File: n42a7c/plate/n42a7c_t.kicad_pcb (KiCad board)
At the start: 2 copper layers, 265.5 x 105.1 mm, 46 parts, among them SW1 CPG151101S11-16, SW10 CPG151101S11-16, SW11 CPG151101S11-16, SW12 CPG151101S11-16, SW13 CPG151101S11-16, SW14 CPG151101S11-16, SW15 CPG151101S11-16, SW16 CPG151101S11-16, SW17 CPG151101S11-16, SW18 CPG151101S11-16, SW19 CPG151101S11-16, SW2 CPG151101S11-16, SW20 CPG151101S11-16, SW21 CPG151101S11-16, SW22 CPG151101S11-16, SW23 CPG151101S11-16, SW24 CPG151101S11-16, SW25 CPG151101S11-16, SW26 CPG151101S11-16, SW27 CPG151101S11-16, SW28 CPG151101S11-16, SW29 CPG151101S11-16, SW3 CPG151101S11-16, SW30 CPG151101S11-16, SW31 CPG151101S11-16, SW32 CPG151101S11-16, SW33 CPG151101S11-16, SW34 CPG151101S11-16, SW35 CPG151101S11-16, SW36 CPG151101S11-16, SW37 CPG151101S11-16, SW38 CPG151101S11-16, SW39 CPG151101S11-16, SW4 CPG151101S11-16, SW40 CPG151101S11-16, SW41 CPG151101S11-16, SW42 CPG151101S11-16, SW5 CPG151101S11-16, SW6 CPG151101S11-16, SW7 CPG151101S11-16, SW8 CPG151101S11-16, SW9 CPG151101S11-16

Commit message: create plate / production PCB
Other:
- board text added: "7.0mm spacer"
- board text added: "CON"
- board text added: "M3x5 ramimate"
- board text added: "PHconn SMD"
- board text added: "foot"
- board text removed: "Fn"

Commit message: create plate/production PCB
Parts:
- moved SW35 2.38 mm to (30.4, 105.4)
- moved SW36 2.38 mm to (54.2, 105.4)
- moved SW41 2.38 mm to (238.7, 105.4)
- moved SW42 2.38 mm to (262.5, 105.4)
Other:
- outline, holes or cut-outs redrawn
- board text added: "n42a7c Rev 1.1 Jul. 2025 Designed by @_hatano_"
- board text removed: "n42a7c Rev 1.0 Jun. 2025 Designed by @_hatano_"
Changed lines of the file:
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@@
 	(footprint "cscslib:CPG151101S11_frame"
 		(layer "B.Cu")
-		(at 260.151781 105.370401)
+		(at 262.532592 105.370401)
 		(property "Reference" "SW42"
 			(at 0 0 180)
@@
 	(footprint "cscslib:CPG151101S11_frame"
 		(layer "B.Cu")
-		(at 236.339261 105.370401)
+		(at 238.720112 105.370224)
 		(property "Reference" "SW41"
 			(at 0 0 180)
@@
 	(footprint "cscslib:CPG151101S11_frame"
 		(layer "B.Cu")
-		(at 32.742215 105.370404)
+		(at 30.360912 105.370404)
 		(property "Reference" "SW35"
 			(at 0 0 180)
@@
 	(footprint "cscslib:CPG151101S11_frame"
 		(layer "B.Cu")
-		(at 56.554735 105.370401)
+		(at 54.173432 105.370401)
 		(property "Reference" "SW36"
 			(at 0 0 180)
@@
 	)
 	(gr_circle
-		(center 23.217207 111.323531)
-		(end 27.217207 111.323531)
+		(center 21.431232 111.323344)
+		(end 25.431232 111.323344)
 		(stroke
 			(width 0.15)
@@
 	)
 	(gr_circle
-		(center 269.676789 111.323531)
-		(end 273.676789 111.323531)
+		(center 271.462272 111.323344)
+		(end 275.462272 111.323344)
 		(stroke
 			(width 0.15)
@@
 		)
 		(fill no)
+		(layer "Eco2.User")
+	)
+	(gr_line
+		(start 173.533448 22.621875)
+		(end 155.078776 22.621875)
+		(stroke
+			(width 0.15)
+			(type solid)
+		)
 		(layer "Eco2.User")
 	)
@@
 	(gr_line
 		(start 252.114181 117.276667)
-		(end 273.843481 117.276466)
+		(end 276.224768 117.276466)
 		(stroke
 			(width 0.15)
@@
 	(gr_line
 		(start 279.201797 97.036019)
-		(end 274.439293 116.68151)
+		(end 276.82008 116.68151)
 		(stroke
 			(width 0.15)
@@
 	)
 	(gr_arc
-		(start 19.049886 117.270465)
-		(mid 18.628987 117.096118)
-		(end 18.454639 116.675221)
+		(start 16.668722 117.276417)
+		(mid 16.247823 117.10207)
+		(end 16.073475 116.681173)
 		(stroke
 			(width 0.15)
@@
 	(gr_line
 		(start 40.78259 117.27626)
-		(end 19.049886 117.270464)
+		(end 16.668736 117.270464)
 		(stroke
 			(width 0.15)
@@
 	)
 	(gr_arc
-		(start 274.439268 116.681329)
-		(mid 274.264716 117.102069)
-		(end 273.843955 117.276642)
+		(start 276.820736 116.681881)
+		(mid 276.646184 117.102621)
+		(end 276.225423 117.277194)
 		(stroke
 			(width 0.15)
@@
 	(gr_line
 		(start 13.692199 97.036019)
-		(end 18.454638 116.6753)
+		(end 16.073424 116.675221)
 		(stroke
 			(width 0.15)
@@
 		(layer "Edge.Cuts")
 	)
-	(gr_text "n42a7c Rev 1.0 Jun. 2025\nDesigned by @_hatano_"
+	(gr_text "n42a7c Rev 1.1 Jul. 2025\nDesigned by @_hatano_"
 		(at 204.192359 36.314113 0)
 		(layer "F.SilkS")
@@
 		(layer "Dwgs.User")
 		(pts
-			(xy 196.750616 22.621875) (xy 248.245104 127.695054)
+			(xy 199.131427 22.621875) (xy 250.625915 127.695054)
 		)
 		(height 88.999144)
@@
 		)
 		(gr_text "105.07"
-			(at 284.59976 75.158465 90)
-			(layer "Dwgs.User")
-			(effects
+			(at 286.980571 75.158465 90)
+			(layer "Dwgs.User")
+			(effects

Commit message: create production plate
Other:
- outline, holes or cut-outs redrawn
- board text added: "JLCJLCJLCJLC"
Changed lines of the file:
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@@
 		(layer "F.SilkS")
+	)
+	(gr_circle
+		(center 175.914696 23.217168)
+		(end 175.61704 23.217168)
+		(stroke
+			(width 0.15)
+			(type solid)
+		)
+		(fill yes)
+		(layer "B.SilkS")
 	)
 	(gr_poly
@@
 	)
 	(gr_circle
-		(center 183.356096 36.611688)
-		(end 183.951408 36.611688)
-		(stroke
-			(width 0.1)
-			(type default)
-		)
-		(fill no)
-		(layer "Cmts.User")
-	)
-	(gr_circle
-		(center 185.210784 37.611688)
-		(end 185.737343 37.611688)
-		(stroke
-			(width 0.1)
-			(type solid)
-		)
-		(fill no)
-		(layer "Cmts.User")
-	)
-	(gr_circle
 		(center 153.590625 104.775)
 		(end 154.781252 104.775002)
@@
 		(layer "Eco2.User")
 	)
-	(gr_rect
-		(start 175.060784 32.011688)
-		(end 187.060784 41.211688)
-		(stroke
-			(width 0.15)
-			(type solid)
-		)
-		(fill no)
-		(locked yes)
-		(layer "Eco2.User")
-	)
 	(gr_circle
 		(center 269.081476 41.67191)
@@
 		(layer "Eco2.User")
 	)
+	(gr_line
+		(start 173.533448 44.053088)
+		(end 173.533449 22.621856)
+		(stroke
+			(width 0.15)
+			(type solid)
+		)
+		(layer "Eco2.User")
+	)
 	(gr_circle
 		(center 21.431232 111.323344)
@@
 	)
 	(gr_rect
-		(start 175.060784 33.161688)
-		(end 187.060784 40.061688)
+		(start 175.656096 33.161688)
+		(end 187.656096 40.061688)
 		(stroke
 			(width 0.15)
@@
 		(start 237.827144 35.71872)
 		(end 230.088088 35.718779)
+		(stroke
+			(width 0.15)
+			(type solid)
+		)
+		(layer "Eco2.User")
+	)
+	(gr_line
+		(start 155.078776 22.621856)
+		(end 155.078776 44.053088)
 		(stroke
 			(width 0.15)
@@
 	)
 	(gr_line
-		(start 173.533448 22.621875)
-		(end 155.078776 22.621875)
+		(start 155.078776 44.053088)
+		(end 173.533448 44.053088)
 		(stroke
 			(width 0.15)
@@
 	)
 	(gr_line
-		(start 173.533448 44.053088)
-		(end 173.533449 22.621856)
-		(stroke
-			(width 0.15)
-			(type solid)
-		)
-		(layer "Edge.Cuts")
-	)
-	(gr_line
 		(start 252.114181 117.276667)
 		(end 276.224768 117.276466)
@@
 	)
 	(gr_line
-		(start 155.078776 22.621856)
-		(end 155.078776 44.053088)
-		(stroke
-			(width 0.15)
-			(type solid)
-		)
-		(layer "Edge.Cuts")
-	)
-	(gr_line
 		(start 96.142888 22.621894)
 		(end 146.446752 22.621894)
@@
 	)
 	(gr_line
+		(start 173.533448 22.621875)
+		(end 155.078776 22.621875)
+		(stroke
+			(width 0.15)
+			(type solid)
+		)
+		(layer "Edge.Cuts")
+	)
+	(gr_line
 		(start 48.540019 117.276628)
 		(end 79.176629 117.276663)
@@
 			(width 0.15)
 			(type default)
-		)
-		(layer "Edge.Cuts")
-	)
-	(gr_line
-		(start 155.078776 44.053088)
-		(end 173.533448 44.053088)
-		(stroke
-			(width 0.15)
-			(type solid)
 		)
 		(layer "Edge.Cuts")
@@
 		)
 	)
-	(gr_text "POWER"
-		(at 180.677192 23.514824 0)
+	(gr_text "JLCJLCJLCJLC"
+		(at 164.30625 27.384375 0)
 		(layer "F.SilkS")
 		(effects
@@
 		)
 	)
-	(gr_text "PON"
-		(at 194.071712 23.81248 0)
-		(layer "F.SilkS" knockout)
+	(gr_text "7.0mm\nspacer"
+		(at 254 144.85 0)
+		(layer "Dwgs.User")
 		(effects
 			(font
@@
 		)
 	)
-	(gr_text "CON"
-		(at 188.416248 23.81248 0)
-		(layer "F.SilkS" knockout)
+	(gr_text "POWER"
+		(at 180.677192 23.514824 0)
+		(layer "Dwgs.User")
 		(effects
 			(font
@@
 		)
 	)
-	(gr_text "7.0mm\nspacer"
-		(at 254 144.85 0)
+	(gr_text "foot"
+		(at 262.5 151.2 0)
 		(layer "Dwgs.User")
 		(effects
@@
 		)
 	)
-	(gr_text "foot"
-		(at 262.5 151.2 0)
-		(layer "Dwgs.User")
+	(gr_text "PON"
+		(at 194.071712 23.81248 0)
+		(layer "Dwgs.User" knockout)
 		(effects
 			(font
@@
 		(effects
 			(font
+				(size 1 1)
+				(thickness 0.15)
+			)
+		)
+	)
+	(gr_text "CON"
+		(at 188.416248 23.81248 0)
+		(layer "Dwgs.User" knockout)
+		(effects
+			(font

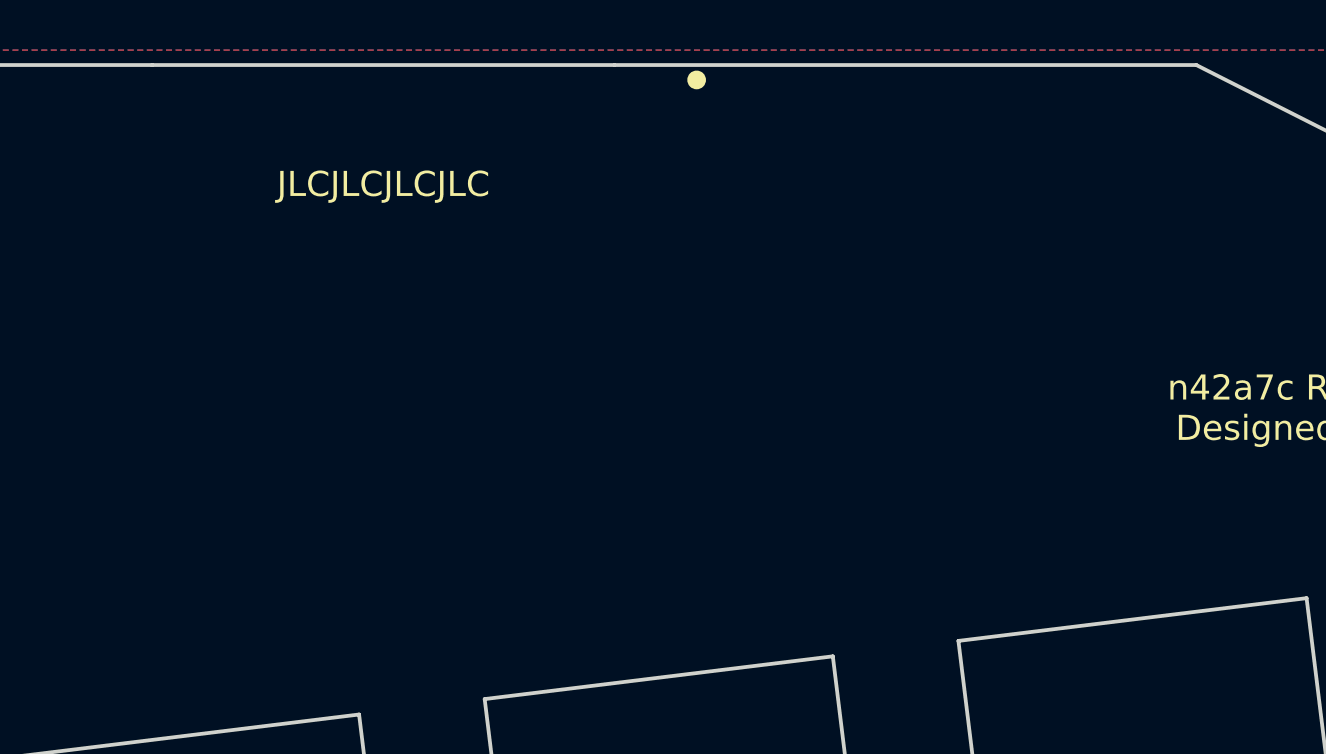
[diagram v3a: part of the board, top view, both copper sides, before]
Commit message: revise Power Conn
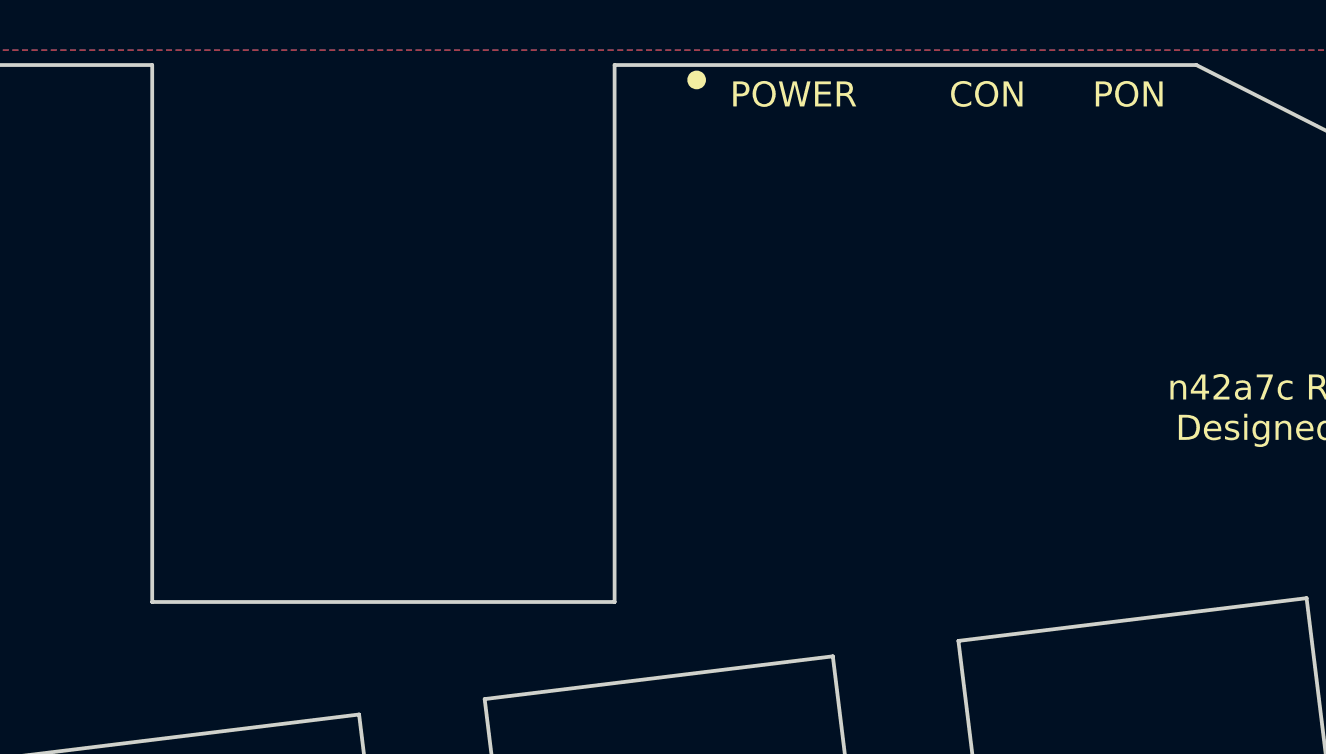
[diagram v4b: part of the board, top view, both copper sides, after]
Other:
- outline, holes or cut-outs redrawn
- board text removed: "JLCJLCJLCJLC"
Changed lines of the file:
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@@
 		(at 176.022952 111.617325 7)
 		(property "Reference" "SW39"
-			(at -8.4 -0.000001 187)
+			(at -8.4 -0.000002 187)
 			(layer "B.SilkS")
 			(hide yes)
@@
 		(at 133.521957 111.907493 -7)
 		(property "Reference" "SW38"
-			(at -8.4 0.000001 173)
+			(at -8.4 0.000002 173)
 			(layer "B.SilkS")
 			(hide yes)
@@
 		(layer "Eco2.User")
 	)
-	(gr_line
-		(start 173.533448 44.053088)
-		(end 173.533449 22.621856)
-		(stroke
-			(width 0.15)
-			(type solid)
-		)
-		(layer "Eco2.User")
-	)
 	(gr_circle
 		(center 21.431232 111.323344)
@@
 		(layer "Eco2.User")
 	)
-	(gr_line
-		(start 155.078776 22.621856)
-		(end 155.078776 44.053088)
-		(stroke
-			(width 0.15)
-			(type solid)
-		)
-		(layer "Eco2.User")
-	)
 	(gr_circle
 		(center 23.81252 41.67191)
@@
 		)
 		(fill no)
-		(layer "Eco2.User")
-	)
-	(gr_line
-		(start 155.078776 44.053088)
-		(end 173.533448 44.053088)
-		(stroke
-			(width 0.15)
-			(type solid)
-		)
 		(layer "Eco2.User")
 	)
@@
 	)
 	(gr_line
+		(start 173.533448 44.053088)
+		(end 173.533449 22.621856)
+		(stroke
+			(width 0.15)
+			(type solid)
+		)
+		(layer "Edge.Cuts")
+	)
+	(gr_line
 		(start 252.114181 117.276667)
 		(end 276.224768 117.276466)
@@
 	)
 	(gr_line
+		(start 155.078776 22.621856)
+		(end 155.078776 44.053088)
+		(stroke
+			(width 0.15)
+			(type solid)
+		)
+		(layer "Edge.Cuts")
+	)
+	(gr_line
 		(start 96.142888 22.621894)
 		(end 146.446752 22.621894)
@@
 	)
 	(gr_line
-		(start 173.533448 22.621875)
-		(end 155.078776 22.621875)
-		(stroke
-			(width 0.15)
-			(type solid)
-		)
-		(layer "Edge.Cuts")
-	)
-	(gr_line
 		(start 48.540019 117.276628)
 		(end 79.176629 117.276663)
@@
 			(width 0.15)
 			(type default)
+		)
+		(layer "Edge.Cuts")
+	)
+	(gr_line
+		(start 155.078776 44.053088)
+		(end 173.533448 44.053088)
+		(stroke
+			(width 0.15)
+			(type solid)
 		)
 		(layer "Edge.Cuts")
@@
 		)
 	)
-	(gr_text "JLCJLCJLCJLC"
-		(at 164.30625 27.384375 0)
+	(gr_text "POWER"
+		(at 180.677192 23.81248 0)
 		(layer "F.SilkS")
+		(effects
+			(font
+				(size 1 1)
+				(thickness 0.15)
+			)
+		)
+	)
+	(gr_text "PON"
+		(at 194.071712 23.81248 0)
+		(layer "F.SilkS" knockout)
+		(effects
+			(font
+				(size 1 1)
+				(thickness 0.15)
+			)
+		)
+	)
+	(gr_text "CON"
+		(at 188.416248 23.81248 0)
+		(layer "F.SilkS" knockout)
 		(effects
 			(font
@@
 		)
 	)
-	(gr_text "POWER"
-		(at 180.677192 23.514824 0)
-		(layer "Dwgs.User")
-		(effects
-			(font
-				(size 1 1)
-				(thickness 0.15)
-			)
-		)
-	)
 	(gr_text "foot"
 		(at 262.5 151.2 0)
@@
 		)
 	)
-	(gr_text "PON"
-		(at 194.071712 23.81248 0)
-		(layer "Dwgs.User" knockout)
-		(effects
-			(font
-				(size 1 1)
-				(thickness 0.15)
-			)
-		)
-	)
 	(gr_text "M3x5 ramimate"
 		(at 253.95 137.75 0)
@@
 		(effects
 			(font
-				(size 1 1)
-				(thickness 0.15)
-			)
-		)
-	)
-	(gr_text "CON"
-		(at 188.416248 23.81248 0)
-		(layer "Dwgs.User" knockout)
-		(effects
-			(font

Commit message: regen production pcb data
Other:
- outline, holes or cut-outs redrawn
- board text added: "6.5mm spacer"
- board text added: "PHconn"
- board text added: "Socket"
